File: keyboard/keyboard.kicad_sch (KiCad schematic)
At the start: 143 parts, among them J1 USB_C_Receptacle, J2 BANK_35, J3 BANK_33, SW1 SW_Push, U1 ATmega32U4-A, Y1 16MHz

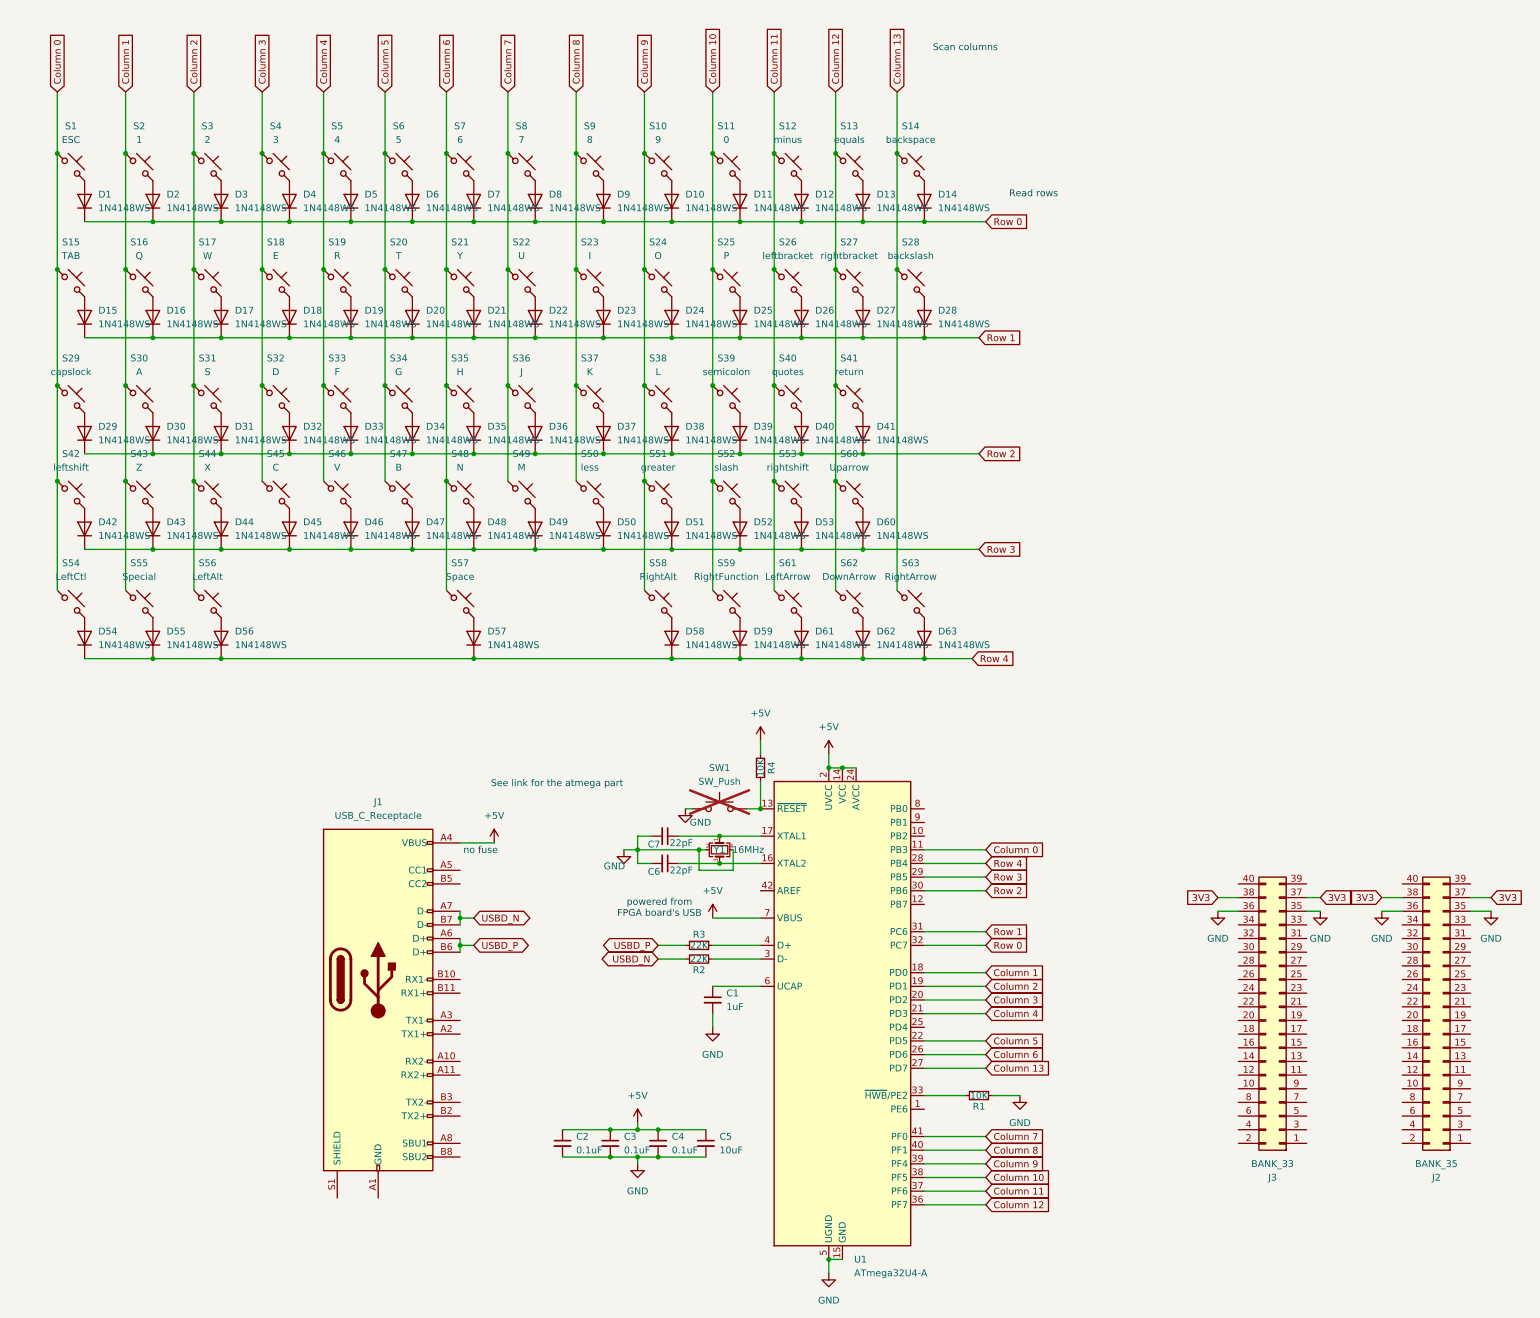
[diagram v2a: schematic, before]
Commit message: Updated keyboard with fixes, also much smaller
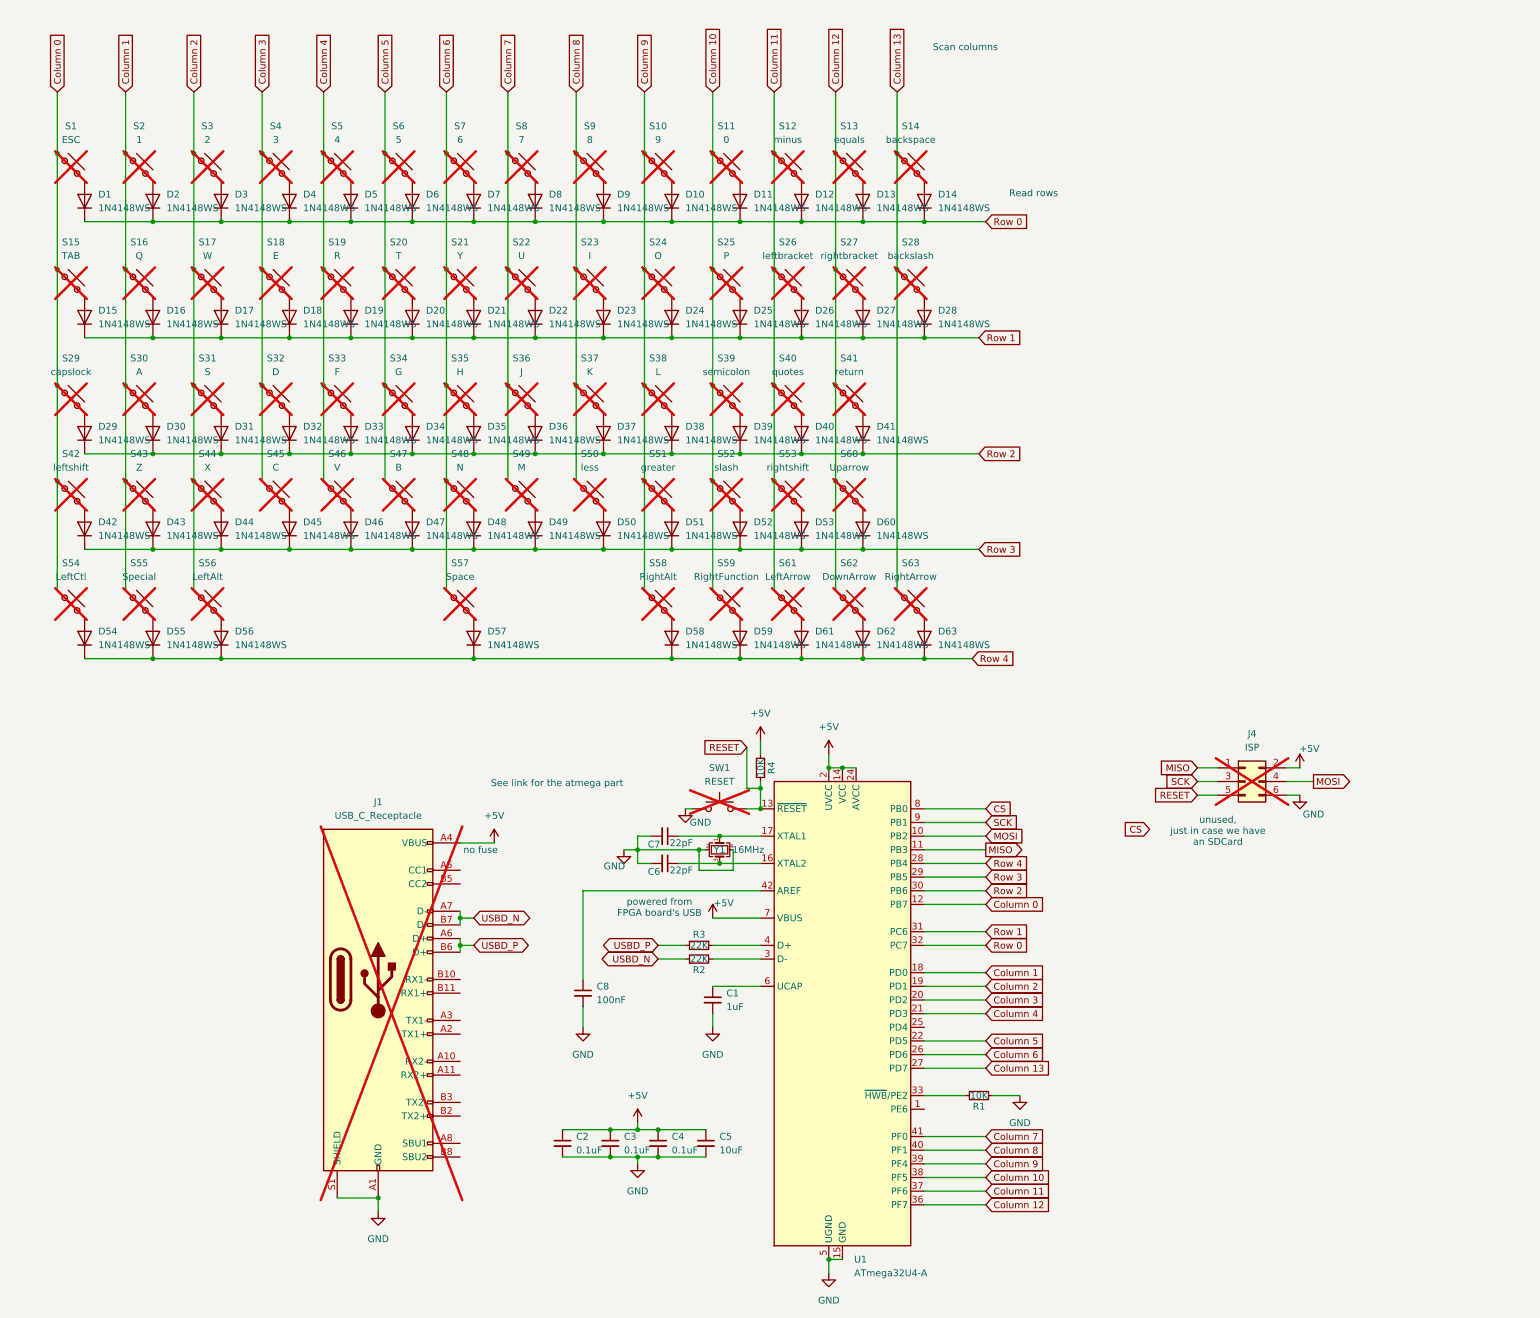
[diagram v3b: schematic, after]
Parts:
- removed J2: BANK_35, Connector_PinHeader_2.54mm:PinHeader_2x20_P2.54mm_Vertical, symbol Connector_Generic:Conn_02x20_Odd_Even
- removed J3: BANK_33, Connector_PinHeader_2.54mm:PinHeader_2x20_P2.54mm_Vertical, symbol Connector_Generic:Conn_02x20_Odd_Even
- added C8: 100nF, Capacitor_SMD:C_0805_2012Metric, symbol Device:C_Small
- added J4: ISP, Connector_PinHeader_2.54mm:PinHeader_2x03_P2.54mm_Vertical, symbol Connector_Generic:Conn_02x03_Odd_Even
- J1, S1, S10, S11, S12, S13, S14, S15, S16, S17, S18, S19, S2, S20, S21, S22, S23, S24, S25, S26, S27, S28, S29, S3, S30, S31, S32, S33, S34, S35, S36, S37, S38, S39, S4, S40, S41, S42, S43, S44, S45, S46, S47, S48, S49, S5, S50, S51, S52, S53, S54, S55, S56, S57, S58, S59, S6, S60, S61, S62, S63, S7, S8, S9: now not fitted
- SW1: value SW_Push -> RESET
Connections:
- net +5V: now also J4.2 (Pin_2)
- net Column 0: now also U1.12 (PB7); no longer U1.11 (PB3)
- net GND: now also J1.A1 (GND), J1.A12 (GND), J1.B1 (GND), J1.B12 (GND), J1.S1 (SHIELD), C8.2, J4.6 (Pin_6)
- net RESET: now reaches R4.1, SW1.2, U1.13 (~{RESET})
- net RESET: now also J4.5 (Pin_5)
- net MOSI: now reaches U1.10 (PB2)
- net MOSI: now also J4.4 (Pin_4)
- net at U1.42 (AREF): now also C8.1
- net CS: now reaches U1.8 (PB0)
- net SCK: now reaches U1.9 (PB1)
- net SCK: now also J4.3 (Pin_3)
- new net MISO: J4.1 (Pin_1), U1.11 (PB3)
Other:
- note added: "unused, just in case we have an SDCard"

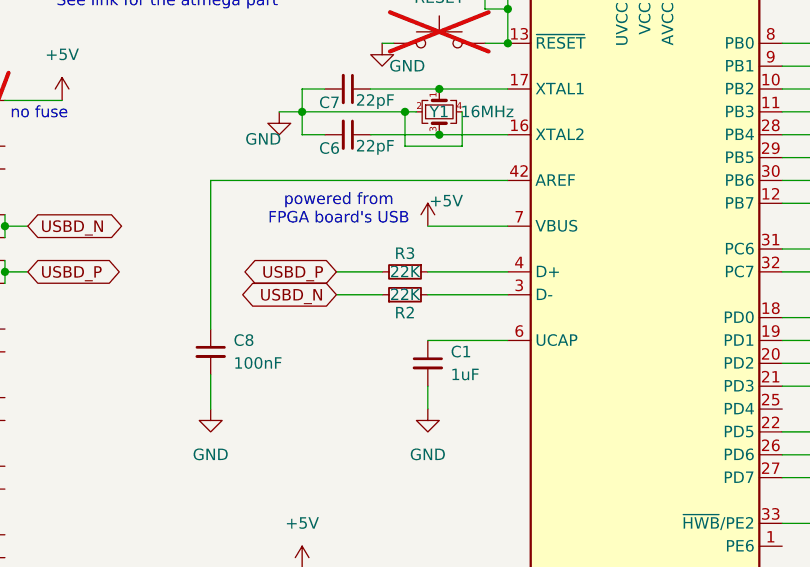
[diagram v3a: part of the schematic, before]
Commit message: Updated keyboard layout and firmware Typing this from the new keyboard :)
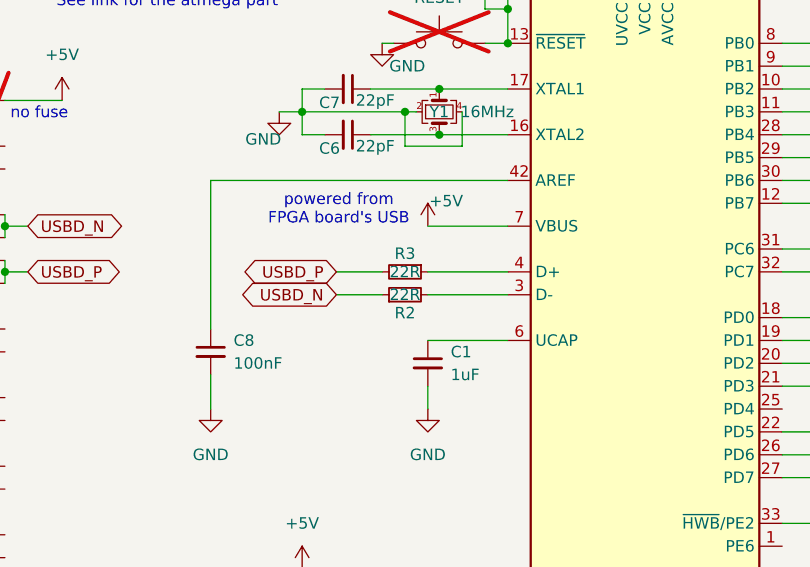
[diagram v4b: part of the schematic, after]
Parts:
- R2, R3: value 22K -> 22R
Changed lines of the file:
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@@
 			)
 		)
-		(property "Value" "22K"
+		(property "Value" "22R"
 			(at 173.99 194.31 90)
 			(effects
@@
 			)
 		)
-		(property "Value" "22K"
+		(property "Value" "22R"
 			(at 173.99 196.85 90)
 			(effects

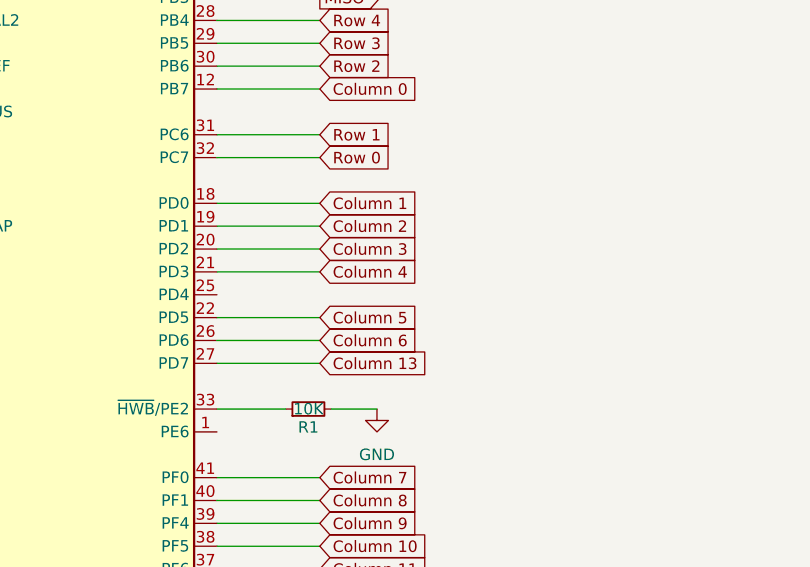
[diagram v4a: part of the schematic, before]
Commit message: More fixes to the keyboard pcb
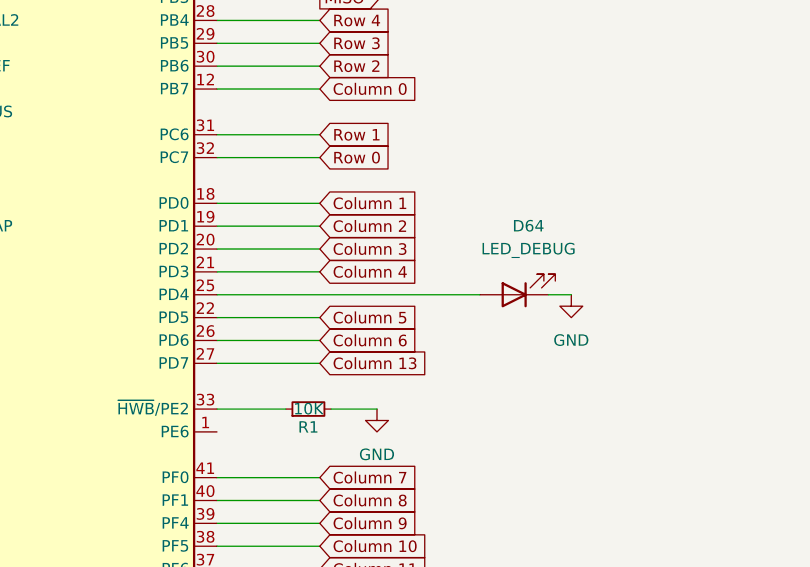
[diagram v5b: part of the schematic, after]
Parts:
- added D64: LED_DEBUG, LED_SMD:LED_1206_3216Metric, symbol Device:LED
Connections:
- net GND: now also D64.1 (K)
- net at U1.25 (PD4): now also D64.2 (A)
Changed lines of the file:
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@@
 	(wire
 		(pts
+			(xy 215.9 209.55) (xy 245.11 209.55)
+		)
+		(stroke
+			(width 0)
+			(type default)
+		)
+	)
+	(wire
+		(pts
 			(xy 227.33 214.63) (xy 215.9 214.63)
 		)
@@
 	(wire
 		(pts
+			(xy 252.73 209.55) (xy 255.27 209.55)
+		)
+		(stroke
+			(width 0)
+			(type default)
+		)
+	)
+	(wire
+		(pts
 			(xy 215.9 222.25) (xy 223.52 222.25)
 		)
@@
 	)
 	(symbol
+		(lib_id "power:GND")
+		(at 255.27 209.55 0)
+		(unit 1)
+		(exclude_from_sim no)
+		(in_bom yes)
+		(on_board yes)
+		(dnp no)
+		(fields_autoplaced yes)
+		(property "Reference" "#PWR012"
+			(at 255.27 215.9 0)
+			(effects
+				(font
+					(size 1.27 1.27)
+				)
+				(hide yes)
+			)
+		)
+		(property "Value" "GND"
+			(at 255.27 214.63 0)
+			(effects
+				(font
+					(size 1.27 1.27)
+				)
+			)
+		)
+		(property "Footprint" ""
+			(at 255.27 209.55 0)
+			(effects
+				(font
+					(size 1.27 1.27)
+				)
+				(hide yes)
+			)
+		)
+		(property "Datasheet" ""
+			(at 255.27 209.55 0)
+			(effects
+				(font
+					(size 1.27 1.27)
+				)
+				(hide yes)
+			)
+		)
+		(property "Description" "Power symbol creates a global label with name \"GND\" , ground"
+			(at 255.27 209.55 0)
+			(effects
+				(font
+					(size 1.27 1.27)
+				)
+				(hide yes)
+			)
+		)
+		(pin "1"
+		)
+		(instances
+			(project "keyboard"
+				(path "/7d6c198a-735f-4c93-baa2-078ce01909c3"
+					(reference "#PWR012")
+					(unit 1)
+				)
+			)
+		)
+	)
+	(symbol
 		(lib_id "ScottoKeebs:Placeholder_Diode")
 		(at 85.09 55.88 90)
@@
 					(unit 1)
 				)
+			)
+		)
+	)
+	(symbol
+		(lib_id "Device:LED")
+		(at 248.92 209.55 180)
+		(unit 1)
+		(exclude_from_sim no)
+		(in_bom yes)
+		(on_board yes)
+		(dnp no)
+		(fields_autoplaced yes)
+		(property "Reference" "D64"
+			(at 250.5075 201.93 0)
+			(effects
+				(font
+					(size 1.27 1.27)
+				)
+			)
+		)
+		(property "Value" "LED_DEBUG"
+			(at 250.5075 204.47 0)
+			(effects
+				(font
+					(size 1.27 1.27)
+				)
+			)
+		)
+		(property "Footprint" "LED_SMD:LED_1206_3216Metric"
+			(at 248.92 209.55 0)
+			(effects
+				(font
+					(size 1.27 1.27)
+				)
+				(hide yes)
+			)
+		)
+		(property "Datasheet" "~"
+			(at 248.92 209.55 0)
+			(effects
+				(font
+					(size 1.27 1.27)
+				)
+				(hide yes)
+			)
+		)
+		(property "Description" "Light emitting diode"
+			(at 248.92 209.55 0)
+			(effects
+				(font
+					(size 1.27 1.27)
+				)
+				(hide yes)
+			)
+		)
+		(pin "2"
+		)
+		(pin "1"
+		)
+		(instances
+			(project ""
+				(path "/7d6c198a-735f-4c93-baa2-078ce01909c3"
+					(reference "D64")
+					(unit 1)
+				)
